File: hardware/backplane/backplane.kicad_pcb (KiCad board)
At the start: 2 copper layers, 100 x 100 mm, 73 parts, among them J1 Screw_Terminal_01x02, J10 RJ45_LED, J11 RJ45_LED, J2 Raspberry_Pi_2_3, J3 Screw_Terminal_01x02, J4 Screw_Terminal_01x03, J5 RJ45_LED, J6 RJ45_LED, J7 Conn_01x08_Female, J8 Conn_02x08_Odd_Even, J9 Conn_02x08_Odd_Even, Q1 Q_NMOS_GSD, Q2 Q_NMOS_GSD, Q3 Q_NMOS_GSD, Q4 Q_NMOS_GSD, U1 TJA1051T, U2 MCP2515-xSO, U3 PAM8403, U4 MCP23017_SO, Y1 8MHz

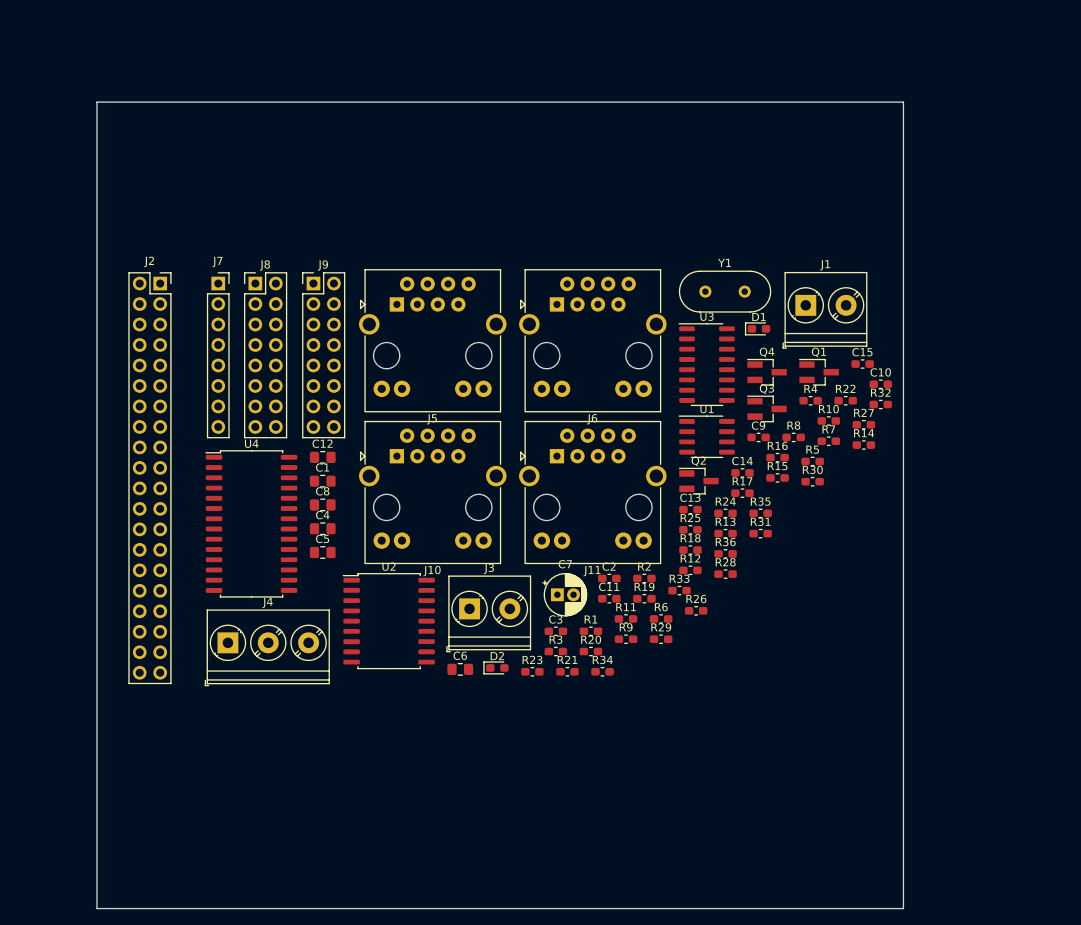
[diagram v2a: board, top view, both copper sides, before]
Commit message: First revision of PCB layout for backplane v2
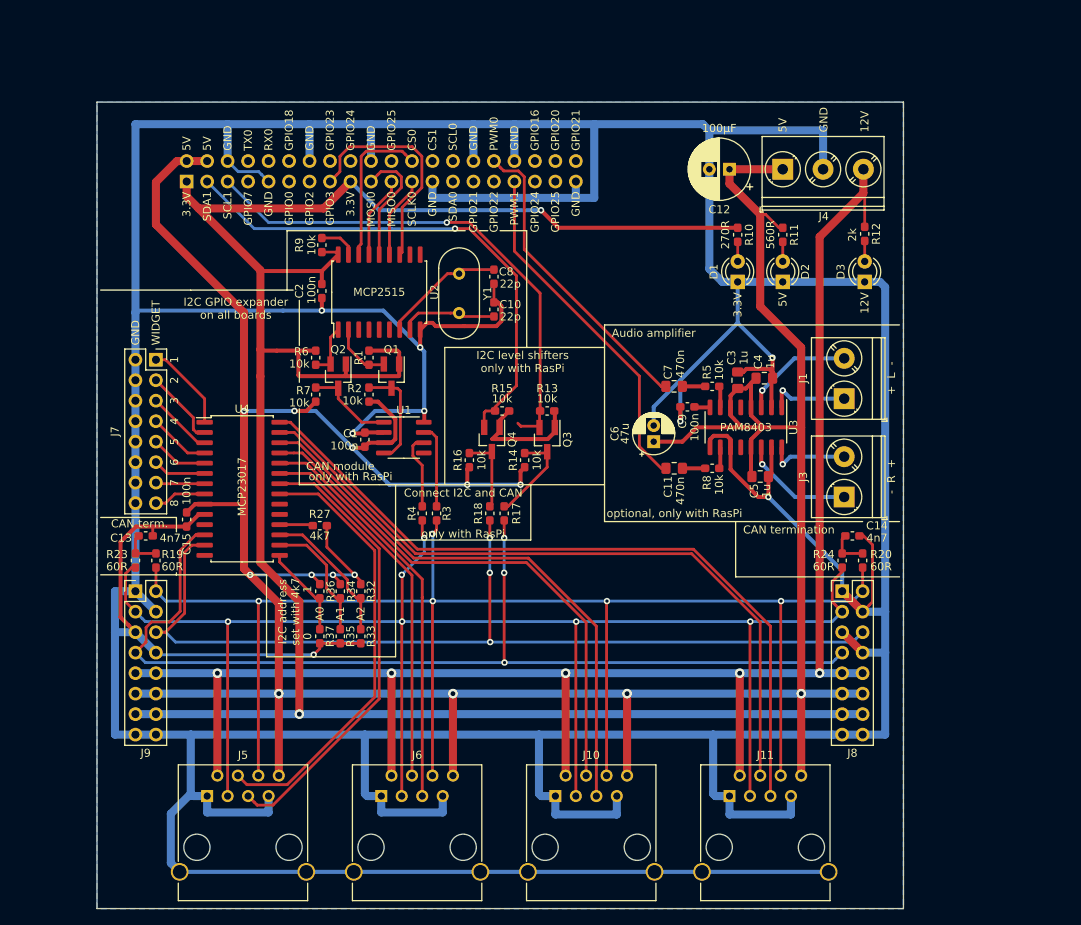
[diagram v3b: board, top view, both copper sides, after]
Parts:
- removed R21, R25, R28, R29, R30: 560R, Resistor_SMD:R_0603_1608Metric_Pad1.05x0.95mm_HandSolder
- removed R22: 60R, Resistor_SMD:R_0603_1608Metric_Pad1.05x0.95mm_HandSolder
- removed R26, R31: 4K7, Resistor_SMD:R_0603_1608Metric_Pad1.05x0.95mm_HandSolder
- added D3: LED, LED_THT:LED_D3.0mm, F.Cu at (155.2, 82.3)
- added R37: 4K7, Resistor_SMD:R_0603_1608Metric_Pad1.05x0.95mm_HandSolder, F.Cu at (87.6, 126.2)
- C1: value 10u -> 100n; footprint Capacitor_SMD:C_0805_2012Metric_Pad1.15x1.40mm_HandSolder -> Capacitor_SMD:C_0603_1608Metric_Pad1.05x0.95mm_HandSolder
- C10: value 100n -> 22p
- C11: value 22p -> 470n; footprint Capacitor_SMD:C_0603_1608Metric_Pad1.05x0.95mm_HandSolder -> Capacitor_SMD:C_0805_2012Metric_Pad1.15x1.40mm_HandSolder
- C12: value 470n -> 100u; footprint Capacitor_SMD:C_0805_2012Metric_Pad1.15x1.40mm_HandSolder -> Capacitor_THT:CP_Radial_D7.5mm_P2.50mm
- C3: value 100n -> 1u; footprint Capacitor_SMD:C_0603_1608Metric_Pad1.05x0.95mm_HandSolder -> Capacitor_SMD:C_0805_2012Metric_Pad1.15x1.40mm_HandSolder
- C6: value 1u -> 47u; footprint Capacitor_SMD:C_0805_2012Metric_Pad1.15x1.40mm_HandSolder -> Capacitor_THT:CP_Radial_D5.0mm_P2.00mm
- C7: value 47u -> 470n; footprint Capacitor_THT:CP_Radial_D5.0mm_P2.00mm -> Capacitor_SMD:C_0805_2012Metric_Pad1.15x1.40mm_HandSolder
- C8: value 470n -> 22p; footprint Capacitor_SMD:C_0805_2012Metric_Pad1.15x1.40mm_HandSolder -> Capacitor_SMD:C_0603_1608Metric_Pad1.05x0.95mm_HandSolder
- C9: value 22p -> 100n
- D1, D2: footprint LED_SMD:LED_0603_1608Metric_Pad1.05x0.95mm_HandSolder -> LED_THT:LED_D3.0mm
- J10, J11, J5, J6: value RJ45_LED -> RJ45; footprint Connector_RJ:RJ45_BEL_SS74301-00x_Vertical -> RJ45_5224:RJ45_5224
- J2: moved to B.Cu
- J7: value Conn_01x08_Female -> Conn_02x08_Top_Bottom; footprint Connector_PinSocket_2.54mm:PinSocket_1x08_P2.54mm_Vertical -> Connector_PinSocket_2.54mm:PinSocket_2x08_P2.54mm_Vertical
- R10: value 560R -> 270R
- R11: value 2k -> 560R
- R12: value 10k -> 2k
- R16: value 0R -> 10k
- R18: value 60R -> 0R
- R20, R24: value 560R -> 60R
- R27: value 560R -> 4K7
- moved J4 90.4 mm to (145.0, 68.3)
- moved C15 86.0 mm to (71.1, 111.8), turned to 270 degrees
- moved J8 82.2 mm to (152.4, 120.7)
- moved R27 68.6 mm to (87.6, 112.5)
- moved R32 68.5 mm to (92.7, 120.7), turned to 90 degrees
- moved C13 67.6 mm to (66.0, 113.8)
- moved J5 65.3 mm to (73.7, 146.1)
- moved J6 64.7 mm to (95.2, 146.1)
- moved R7 63.9 mm to (87.1, 96.3), turned to 90 degrees
- moved C12 61.8 mm to (138.4, 68.3), turned to 180 degrees
- moved R9 61.7 mm to (87.9, 77.7), turned to 90 degrees
- moved R19 60.8 mm to (67.3, 116.8), turned to 90 degrees
- moved D2 59.5 mm to (145.0, 82.3), turned to 90 degrees
- moved C4 57.8 mm to (142.7, 94.2)
- moved C5 55.1 mm to (142.2, 106.4)
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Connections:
- C1 pad 1: +3V3 -> VCC
- C11 pad 2: GND -> AUDIO_R
- C12 pad 1: Net-(C12-Pad1) -> VCC
- C12 pad 2: AUDIO_R -> GND
- C2 pad 1: VCC -> +3V3
- C3 pad 1: +3V3 -> VCC
- C7 pad 1: VCC -> Net-(C7-Pad1)
- C7 pad 2: GND -> AUDIO_L
- C8 pad 2: AUDIO_L -> GND
- J7 pad 2: Net-(J7-Pad2) -> GND
- J7 pad 4: Net-(J7-Pad4) -> GND
- J7 pad 6: Net-(J7-Pad6) -> GND
- J7 pad 8: Net-(J7-Pad8) -> GND
- J8 pad 15: Net-(J8-Pad15) -> GND
- J8 pad 16: Net-(J8-Pad16) -> GND
- J9 pad 15: Net-(J9-Pad15) -> GND
- J9 pad 16: Net-(J9-Pad16) -> GND
- R10 pad 1: VCC -> +3V3
- R11 pad 1: +12V -> VCC
- R12 pad 1: +3V3 -> +12V
- R12 pad 2: SCL_3V3 -> Net-(D3-Pad2)
- R13 pad 1: VCC -> +3V3
- R13 pad 2: Net-(Q3-Pad3) -> SCL_3V3
- R14 pad 1: +3V3 -> VCC
- R14 pad 2: SDA_3V3 -> Net-(Q3-Pad3)
- R15 pad 1: VCC -> +3V3
- R15 pad 2: Net-(Q4-Pad3) -> SDA_3V3
- R16 pad 1: SCL -> VCC
- R16 pad 2: Net-(Q3-Pad3) -> Net-(Q4-Pad3)
- R17 pad 1: SDA -> SCL
- R17 pad 2: Net-(Q4-Pad3) -> Net-(Q3-Pad3)
- R18 pad 1: CAN_H -> SDA
- R18 pad 2: Net-(C13-Pad1) -> Net-(Q4-Pad3)
- R19 pad 2: Net-(C14-Pad1) -> Net-(C13-Pad1)
- R20 pad 1: VCC -> CAN_H
- R20 pad 2: Net-(J5-Pad10) -> Net-(C14-Pad1)
- R23 pad 2: Net-(C14-Pad1) -> Net-(C13-Pad1)
- R24 pad 1: VCC -> CAN_L
- R24 pad 2: Net-(J5-Pad12) -> Net-(C14-Pad1)
- R27 pad 1: VCC -> Net-(R27-Pad1)
- R27 pad 2: Net-(J10-Pad10) -> VCC
- R32 pad 1: Net-(R31-Pad1) -> /GPIO_A2
- R32 pad 2: GND -> VCC
- R33 pad 1: Net-(R33-Pad1) -> /GPIO_A2
- R33 pad 2: VCC -> GND
- R34 pad 1: Net-(R33-Pad1) -> /GPIO_A1
- R34 pad 2: GND -> VCC
- R35 pad 1: Net-(R35-Pad1) -> /GPIO_A1
- R35 pad 2: VCC -> GND
- R36 pad 1: Net-(R35-Pad1) -> /GPIO_A0
- R36 pad 2: GND -> VCC
- R5 pad 2: Net-(C8-Pad1) -> Net-(C7-Pad1)
- R8 pad 2: Net-(C12-Pad1) -> Net-(C11-Pad1)
- U1 pad 8: Net-(U1-Pad8) -> GND
- U2 pad 7: Net-(C9-Pad1) -> Net-(C8-Pad1)
- U2 pad 8: Net-(C11-Pad1) -> Net-(C10-Pad1)
- U3 pad 8: Net-(C10-Pad1) -> Net-(C9-Pad1)
- U4 pad 15: Net-(R35-Pad1) -> /GPIO_A0
- U4 pad 16: Net-(R33-Pad1) -> /GPIO_A1
- U4 pad 17: Net-(R31-Pad1) -> /GPIO_A2
- U4 pad 18: Net-(R26-Pad1) -> Net-(R27-Pad1)
- U4 pad 2: Net-(J7-Pad2) -> Net-(J7-Pad3)
- U4 pad 21: MODULE_ENABLE_0 -> MODULE_READY_0
- U4 pad 22: MODULE_ENABLE_1 -> MODULE_ENABLE_0
- U4 pad 23: MODULE_ENABLE_2 -> MODULE_READY_1
- U4 pad 24: MODULE_ENABLE_3 -> MODULE_ENABLE_1
- U4 pad 25: MODULE_READY_0 -> MODULE_READY_2
- U4 pad 26: MODULE_READY_1 -> MODULE_ENABLE_2
- U4 pad 27: MODULE_READY_2 -> MODULE_READY_3
- U4 pad 28: MODULE_READY_3 -> MODULE_ENABLE_3
- U4 pad 3: Net-(J7-Pad3) -> Net-(J7-Pad5)
- U4 pad 4: Net-(J7-Pad4) -> Net-(J7-Pad7)
- U4 pad 5: Net-(J7-Pad5) -> Net-(J7-Pad9)
- U4 pad 6: Net-(J7-Pad6) -> Net-(J7-Pad11)
- U4 pad 7: Net-(J7-Pad7) -> Net-(J7-Pad13)
- U4 pad 8: Net-(J7-Pad8) -> Net-(J7-Pad15)
- Y1 pad 1: Net-(C9-Pad1) -> Net-(C8-Pad1)
- Y1 pad 2: Net-(C11-Pad1) -> Net-(C10-Pad1)
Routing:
- net GND: track 0.00 -> 846.9 mm, vias 0 -> 8
- net VCC: track 0.00 -> 419.0 mm, vias 0 -> 13
- net +3V3: track 0.00 -> 292.8 mm, vias 0 -> 2
- net +12V: track 0.00 -> 210.0 mm, vias 0 -> 5
- net CAN_L: track 0.00 -> 202.3 mm, vias 0 -> 6
- net CAN_H: track 0.00 -> 191.4 mm, vias 0 -> 5
- net SCL: track 0.00 -> 126.4 mm, vias 0 -> 3
- net SDA: track 0.00 -> 118.7 mm, vias 0 -> 3
- net MODULE_ENABLE_3: track 0.00 -> 92.4 mm
- net MODULE_READY_3: track 0.00 -> 88.4 mm
- net MODULE_ENABLE_2: track 0.00 -> 69.8 mm
- net MODULE_READY_2: track 0.00 -> 65.7 mm
- net SDA_3V3: track 0.00 -> 64.3 mm, vias 0 -> 1
- net SCL_3V3: track 0.00 -> 64.1 mm, vias 0 -> 1
- net MODULE_ENABLE_0: track 0.00 -> 57.5 mm
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- added copper zone on B.Cu, net GND
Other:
- board text added: "+ L -"
- board text added: "- R +"
- board text added: "0"
- board text added: "1"
- board text added: "100n"
- board text added: "100µF"
- board text added: "10k"
- board text added: "12V"
- board text added: "1u"
- board text added: "2"
- board text added: "22p"
- board text added: "270R"
- board text added: "2k"
- board text added: "3"
- board text added: "3.3V"
- board text added: "4"
- board text added: "470n"
- board text added: "47u"
- board text added: "4k7"
- board text added: "4n7"
- board text added: "5"
- board text added: "560R"
- board text added: "5V"
- board text added: "6"
- board text added: "60R"
- board text added: "7"
- board text added: "8"
- board text added: "A0"
- board text added: "A1"
- board text added: "A2"
- board text added: "Audio amplifier"
- board text added: "CAN module"
- board text added: "CAN term."
- board text added: "CAN termination"
- board text added: "CS0"
- board text added: "CS1"
- board text added: "Connect I2C and CAN"
- board text added: "GND"
- board text added: "GPIO0"
- board text added: "GPIO16"
- board text added: "GPIO18"
- board text added: "GPIO2"
- board text added: "GPIO20"
- board text added: "GPIO21"
- board text added: "GPIO22"
- board text added: "GPIO23"
- board text added: "GPIO24"
- board text added: "GPIO25"
- board text added: "GPIO3"
- board text added: "GPIO7"
- board text added: "I2C GPIO expander on all boards"
- board text added: "I2C address set with 4k7"
- board text added: "I2C level shifters only with RasPi"
- board text added: "MCP23017"
- board text added: "MCP2515"
- board text added: "MISO0"
- board text added: "MOSI0"
- board text added: "PAM8403"
- board text added: "PWM0"
- board text added: "PWM1"
- board text added: "RX0"
- board text added: "SCL0"
- board text added: "SCL1"
- board text added: "SCLK0"
- board text added: "SDA0"
- board text added: "SDA1"
- board text added: "TX0"
- board text added: "WIDGET"
- board text added: "only with RasPi"
- board text added: "optional, only with RasPi"

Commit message: Backplane PCB: add audio filter circuit
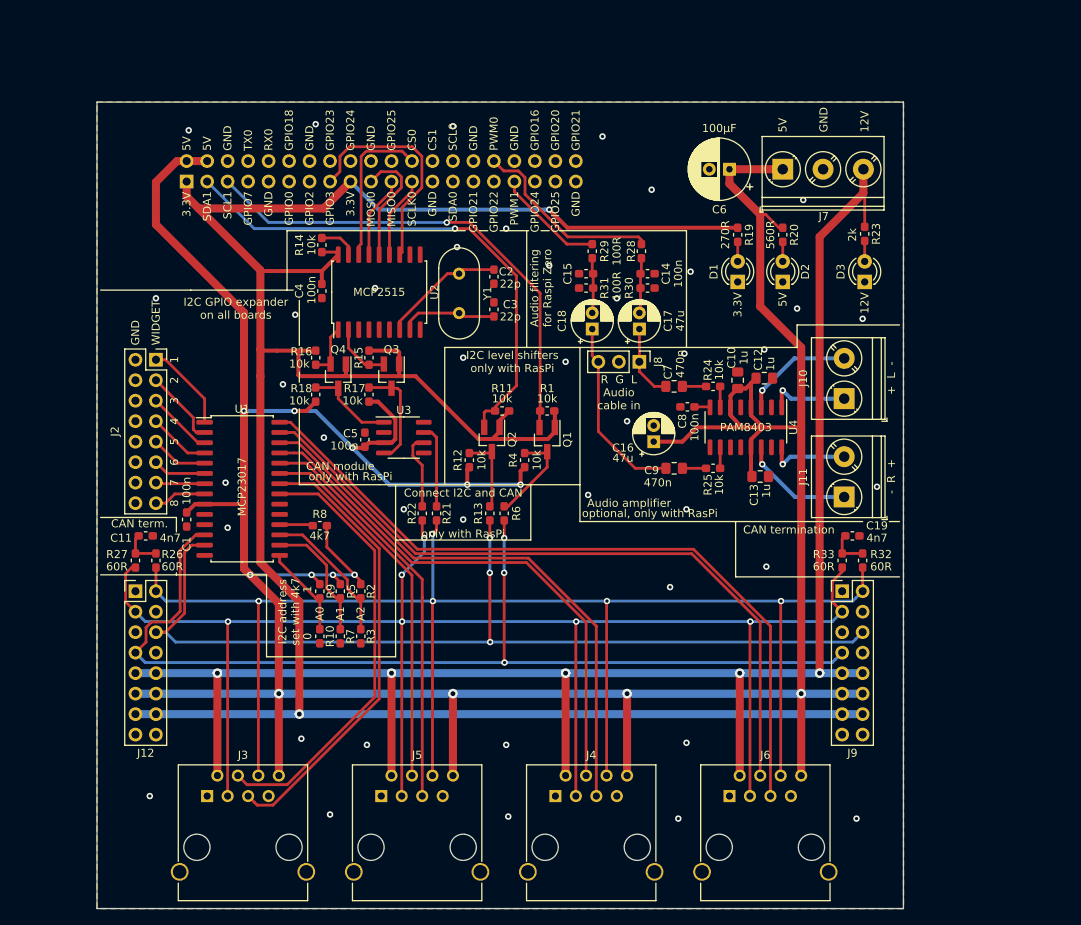
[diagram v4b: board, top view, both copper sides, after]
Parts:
- removed the C11 at (131.6, 105.4)
- removed the C3 at (139.4, 94.5)
- added C10: 1u, Capacitor_SMD:C_0805_2012Metric_Pad1.15x1.40mm_HandSolder, F.Cu at (139.4, 94.5)
- added C14: 100n, Capacitor_SMD:C_0603_1608Metric_Pad1.05x0.95mm_HandSolder, F.Cu at (128.3, 81.3)
- added C15: 100n, Capacitor_SMD:C_0603_1608Metric_Pad1.05x0.95mm_HandSolder, F.Cu at (120.7, 81.3)
- added C17: 47u, Capacitor_THT:CP_Radial_D5.0mm_P2.00mm, F.Cu at (127.3, 88.1)
- added C18: 47u, Capacitor_THT:CP_Radial_D5.0mm_P2.00mm, F.Cu at (121.4, 88.1)
- added C9: 470n, Capacitor_SMD:C_0805_2012Metric_Pad1.15x1.40mm_HandSolder, F.Cu at (131.6, 105.4)
- added J8: Conn_01x03, Connector_PinHeader_2.54mm:PinHeader_1x03_P2.54mm_Vertical, F.Cu at (127.3, 92.2)
- added R28: 100R, Resistor_SMD:R_0603_1608Metric_Pad1.05x0.95mm_HandSolder, F.Cu at (127.5, 78.5)
- added R29: 100R, Resistor_SMD:R_0603_1608Metric_Pad1.05x0.95mm_HandSolder, F.Cu at (121.4, 78.5)
- added R30: 100R, Resistor_SMD:R_0603_1608Metric_Pad1.05x0.95mm_HandSolder, F.Cu at (128.3, 83.1)
- added R31: 100R, Resistor_SMD:R_0603_1608Metric_Pad1.05x0.95mm_HandSolder, F.Cu at (120.7, 83.1)
- moved R24 0.11 mm to (136.4, 95.2)
- moved R25 0.11 mm to (136.4, 105.4)
- renumbered C15 to C1, C13 to C11, C4 to C12, C5 to C13, C6 to C16, C14 to C19, C8 to C2, C10 to C3, C2 to C4, C1 to C5, C12 to C6, C9 to C8, J2 to J1, J1 to J10, J3 to J11, J9 to J12, J7 to J2, J5 to J3, J10 to J4, J6 to J5, J11 to J6, J4 to J7, J8 to J9, Q3 to Q1, Q4 to Q2, Q1 to Q3, Q2 to Q4, R13 to R1, R37 to R10, R15 to R11, R16 to R12, R18 to R13, R9 to R14, R1 to R15, R6 to R16, R2 to R17, R7 to R18, R10 to R19, R32 to R2, R11 to R20, R3 to R21, R4 to R22, R12 to R23, R5 to R24, R8 to R25, R19 to R26, R23 to R27, R33 to R3, R20 to R32, R24 to R33, R14 to R4, R34 to R5, R17 to R6, R35 to R7, R27 to R8, R36 to R9, U4 to U1, U1 to U3, U3 to U4
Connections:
- J1 pad 32: AUDIO_L -> PWM0
- J1 pad 33: AUDIO_R -> PWM1
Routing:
- net GND: track 846.9 -> 0.00 mm, vias 8 -> 41
- net AUDIO_L: track 38.2 -> 9.31 mm
- net PWM0: track 0.00 -> 24.1 mm
- net AUDIO_R: track 43.7 -> 23.3 mm
- net +3V3: track 292.8 -> 307.6 mm
- net PWM1: track 0.00 -> 13.6 mm
- net Net-(C14-Pad1): track 0.00 -> 6.88 mm
- net Net-(C15-Pad1): track 0.00 -> 6.87 mm
- net SCL_3V3: track 64.1 -> 61.2 mm
- added copper zone on F.Cu, net GND
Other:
- board text added: "100R"
- board text added: "Audio filtering for Raspi Zero"
- board text added: "R G L Audio cable in"

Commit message: Backplane PCB: add overvoltage protection, remove some 0Rs, some reorganization
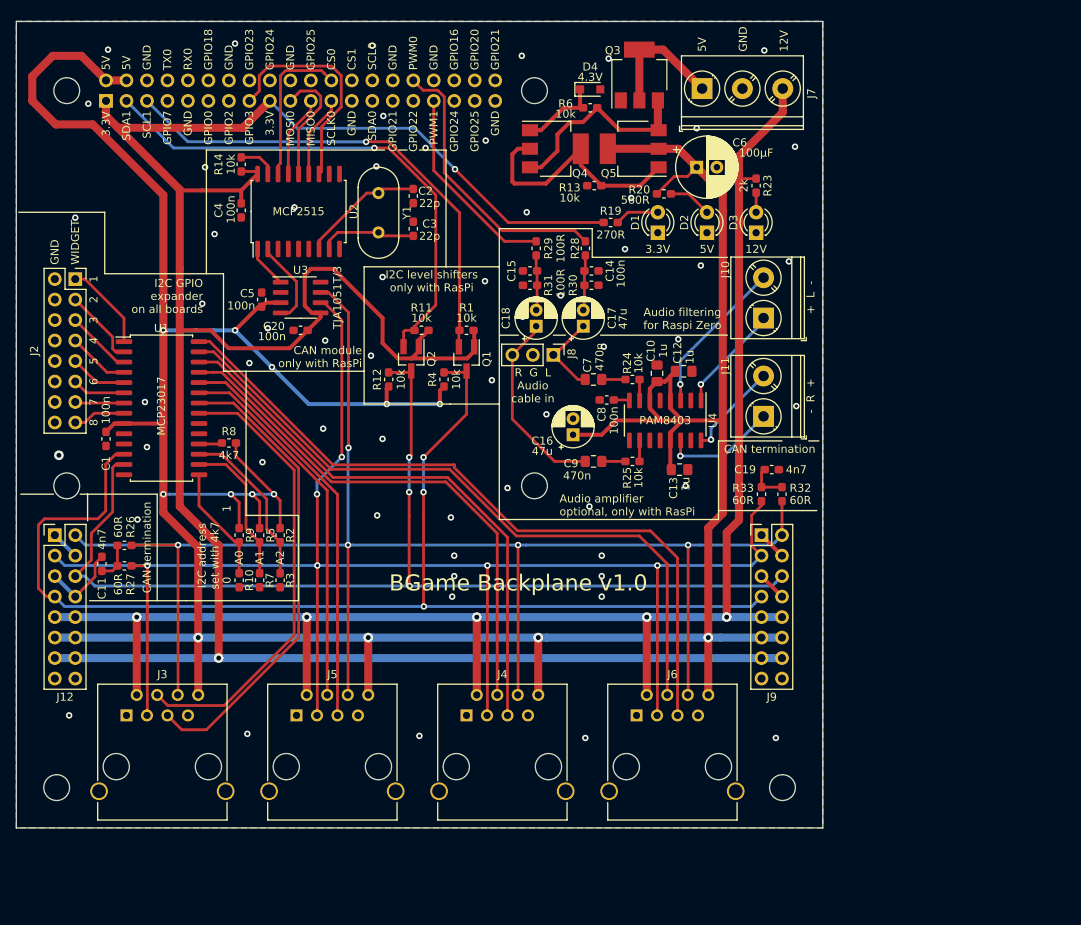
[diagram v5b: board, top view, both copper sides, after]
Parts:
- removed R15, R16, R17, R18: 10k, Resistor_SMD:R_0603_1608Metric_Pad1.05x0.95mm_HandSolder
- removed R21, R22: 0R, Resistor_SMD:R_0603_1608Metric_Pad1.05x0.95mm_HandSolder
- added C20: 100n, Capacitor_SMD:C_0603_1608Metric_Pad1.05x0.95mm_HandSolder, F.Cu at (85.2, 88.3)
- added D4: BZX384-4V3, Diode_SMD:D_SOD-323_HandSoldering, F.Cu at (121.2, 58.4)
- added Q5: ZXMP4A16G, Package_TO_SOT_SMD:SOT-223-3_TabPin2, F.Cu at (126.5, 65.8)
- added REF**: MountingHole_3.2mm_M3, MountingHole:MountingHole_3.2mm_M3, F.Cu at (145.0, 145.0)
- added REF**: MountingHole_3.2mm_M3, MountingHole:MountingHole_3.2mm_M3, F.Cu at (55.0, 145.0)
- added REF**: MountingHole_3.2mm_M3, MountingHole:MountingHole_3.2mm_M3, F.Cu at (56.2, 107.6)
- added REF**: MountingHole_3.2mm_M3, MountingHole:MountingHole_3.2mm_M3, F.Cu at (114.2, 107.6)
- added REF**: MountingHole_3.2mm_M3, MountingHole:MountingHole_3.2mm_M3, F.Cu at (114.2, 58.6)
- added REF**: MountingHole_3.2mm_M3, MountingHole:MountingHole_3.2mm_M3, F.Cu at (56.2, 58.6)
- Q3, Q4: value Q_NMOS_GSD -> ZXMP4A16G; footprint Package_TO_SOT_SMD:SOT-23_Handsoldering -> Package_TO_SOT_SMD:SOT-223-3_TabPin2
- R13, R6: value 0R -> 10k
- U3: value TJA1051T -> TJA1051T/3
- moved R6 51.4 mm to (121.2, 60.7), turned to 180 degrees
- moved Q3 48.4 mm to (127.3, 56.6), turned to 90 degrees
- moved R13 42.7 mm to (121.7, 70.4), turned to 180 degrees
- moved Q4 39.0 mm to (116.8, 65.8), turned to 0 degrees
- moved C5 21.6 mm to (80.4, 84.5)
- moved U3 21.6 mm to (85.2, 84.2)
- moved R19 15.8 mm to (123.7, 74.9), turned to 0 degrees
- moved R20 15.6 mm to (130.3, 71.4), turned to 0 degrees
- moved J6 15.3 mm to (126.9, 136.1)
- moved R8 15.2 mm to (76.4, 102.3)
- moved J4 14.9 mm to (105.8, 136.1)
- moved D3 14.8 mm to (141.7, 76.2)
- moved R23 14.7 mm to (141.7, 70.4)
- moved J5 14.5 mm to (84.7, 136.1)
- moved C1 14.1 mm to (61.1, 101.8)
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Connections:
- J7 pad 1: VCC -> +5V
- Q1 pad 3: Net-(Q1-Pad3) -> SCL
- Q2 pad 3: Net-(Q2-Pad3) -> SDA
- Q3 pad 1: +3V3 -> GND
- Q3 pad 2: Net-(Q3-Pad2) -> +5V
- Q4 pad 1: +3V3 -> Net-(D4-Pad1)
- Q4 pad 3: Net-(Q4-Pad3) -> Net-(Q3-Pad3)
- R12 pad 2: Net-(Q2-Pad3) -> SDA
- R13 pad 1: SDA -> Net-(Q4-Pad2)
- R13 pad 2: Net-(Q2-Pad3) -> GND
- R4 pad 2: Net-(Q1-Pad3) -> SCL
- R6 pad 1: SCL -> Net-(Q3-Pad3)
- R6 pad 2: Net-(Q1-Pad3) -> Net-(D4-Pad1)
- U2 pad 1: Net-(Q4-Pad2) -> Net-(U2-Pad1)
- U2 pad 2: Net-(Q3-Pad2) -> Net-(U2-Pad2)
- U3 pad 1: Net-(Q4-Pad3) -> Net-(U2-Pad1)
- U3 pad 4: Net-(Q3-Pad3) -> Net-(U2-Pad2)
- U3 pad 5: Net-(U3-Pad5) -> +3V3
- U3 pad 6: Net-(R22-Pad2) -> CAN_L
- U3 pad 7: Net-(R21-Pad2) -> CAN_H
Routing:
- net SCL: track 126.4 -> 150.9 mm
- net Net-(Q4-Pad2): track 6.54 -> 29.9 mm
- net GND: track 0.00 -> 20.7 mm, vias 41 -> 59
- net SDA: track 118.7 -> 135.3 mm
- net +5V: track 0.00 -> 16.1 mm
- net CAN_H: track 191.4 -> 206.5 mm
- net Net-(Q1-Pad3): track 12.1 -> 0.00 mm
- net Net-(Q3-Pad3): track 13.2 -> 25.1 mm
- net PWM1: track 13.6 -> 25.0 mm
- net PWM0: track 24.1 -> 35.1 mm
- net Net-(Q4-Pad3): track 11.0 -> 0.00 mm
- net Net-(U2-Pad2): track 0.00 -> 10.8 mm
- net +12V: track 210.0 -> 199.3 mm
- net Net-(R21-Pad2): track 10.4 -> 0.00 mm
- net Net-(D4-Pad1): track 0.00 -> 10.2 mm
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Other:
- board text added: "4.3V"
- board text added: "Audio amplifier optional, only with RasPi"
- board text added: "BGame Backplane v1.0"
- board text added: "CAN module only with RasPi"
- board text added: "No other components on this side"
- board text added: "Raspberry Pi 3B+"
- board text added: "Raspberry Pi Zero W"
- board text added: "TJA1051T/3"
- board text removed: "Audio amplifier"
- board text removed: "CAN module"
- board text removed: "CAN term."
- board text removed: "Connect I2C and CAN"
- board text removed: "only with RasPi"
- board text removed: "optional, only with RasPi"
